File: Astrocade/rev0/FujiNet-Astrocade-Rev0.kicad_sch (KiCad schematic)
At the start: 0 parts

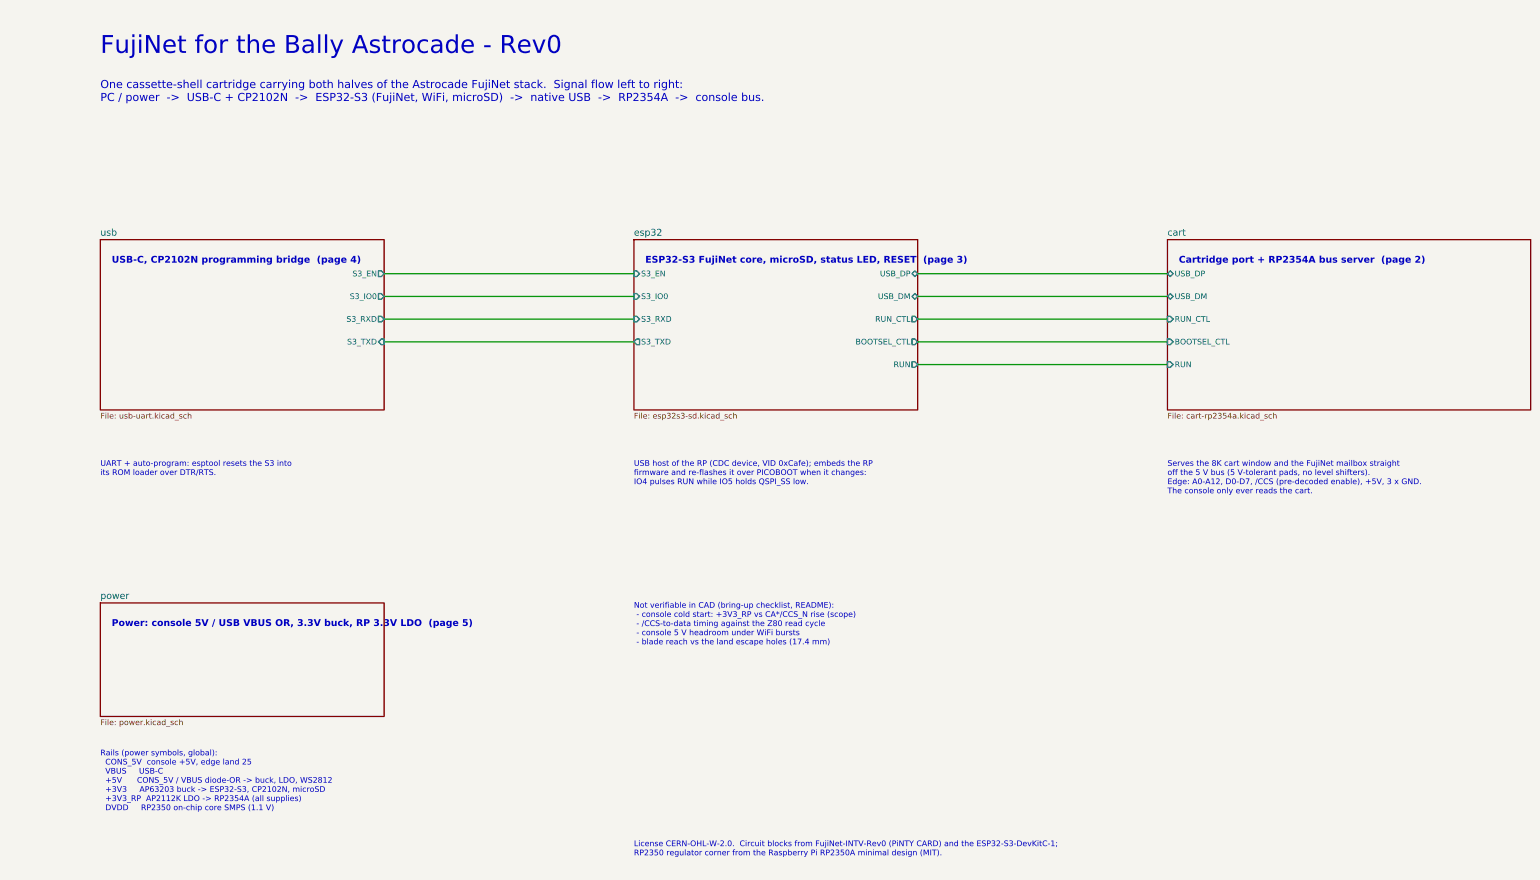
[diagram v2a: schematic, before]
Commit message: Astrocade Rev0: redraw the schematic wired (5200 style), re-audit (#53)
The schematic was readable but disconnected: every edge land and RP GPIO
ended in a label and the RP's decoupling stood in a row away from its pins.
Port the FujiNet-5200 drawing pipeline (sch_draw / sch_draft / sch_place /
netlist) and hand-draw every sheet the way the later carts are drawn:

- root: the board outline at 2:1, each sheet's block over its region, the
  nine inter-sheet signals wired without a crossing
- cart-bus: the 26-land edge straight into the RP2354A's GPIO unit
  (22 parallel wires, no crossings); rp-core: every supply pin wired to
  its own capacitor and rail; fujinet, usb, power: all wired
- RP2354A split into two units; references frozen in tools/refs.lock,
  net names in tools/nets.lock

The routed board is unchanged: tools/sync_pcb_nets.py renames the board's
nets to the new sheet paths (self-checked), sync_pcb_sheets.py re-points
the footprint links. DRC with schematic parity 0/0/0, ERC 0, netlist
parity 74/74, check_nets 182/182; CPL byte-identical, gerbers identical
but for names and dates. build_all.sh now keeps the routed board by
default (LAYOUT=1 re-routes).

Re-audit (design review Part 3, deep review 25/25 gated, datasheets from
the sibling carts): VSENSE divider 100k/150k -> 10k/15k so RP2350-E9 (A2
silicon) cannot hold the serve gate open in a switched-off console (value
change only, same lands). DVDD decoupling, a VBUS pull-down, the activity
LED and the core inductor's stock are Rev1 / bring-up notes.

Co-authored-by: Claude Opus 5.5 <noreply@anthropic.com>
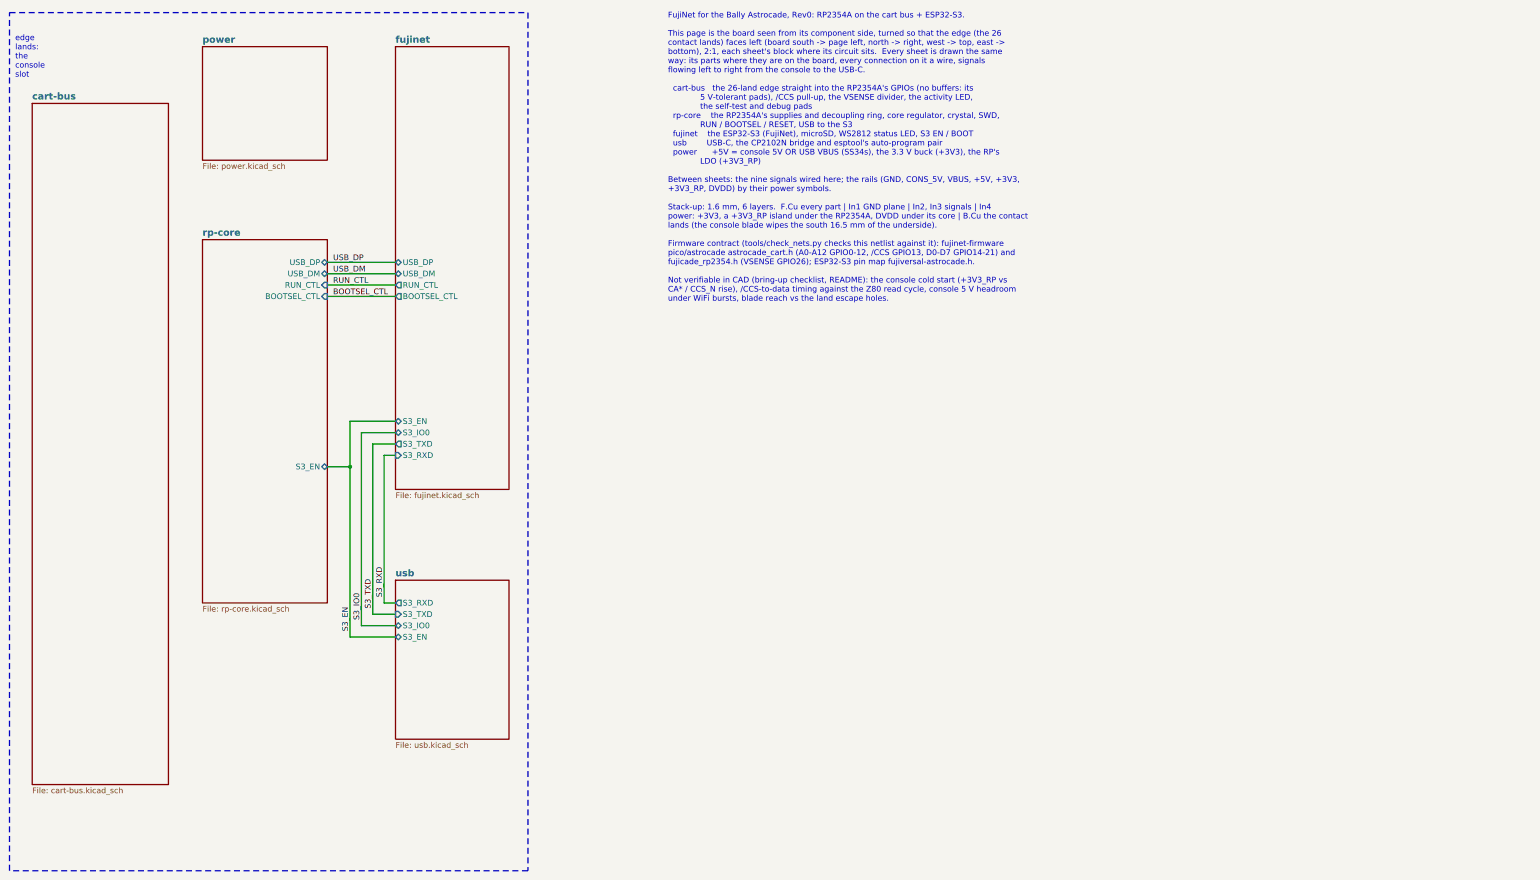
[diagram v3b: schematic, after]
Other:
- removed sheet cart
- removed sheet esp32
- added sheet cart-bus (cart-bus.kicad_sch)
- added sheet fujinet (fujinet.kicad_sch)
- added sheet rp-core (rp-core.kicad_sch)
- sheet usb: file usb-uart.kicad_sch -> usb.kicad_sch
- note added: "FujiNet for the Bally Astrocade, Rev0: RP2354A on the cart bus + ESP32-S3. This page is the board seen from its component side, turned so that the edge (the 26 contact lands) faces left (board south -> page left, north -> right, west -> top, east -> bottom), 2:1, each sheet's block where its circuit sits. Every sheet is drawn the same way: its parts where they are on the board, every connection o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"
- note added: "edge lands: the console slot"
- note removed: "Cartridge port + RP2354A bus server (page 2)"
- note removed: "ESP32-S3 FujiNet core, microSD, status LED, RESET (page 3)"
- note removed: "FujiNet for the Bally Astrocade - Rev0"
- note removed: "License CERN-OHL-W-2.0. Circuit blocks from FujiNet-INTV-Rev0 (PiNTY CARD) and the ESP32-S3-DevKitC-1; RP2350 regulator corner from the Raspberry Pi RP2350A minimal design (MIT)."
- note removed: "Not verifiable in CAD (bring-up checklist, README): - console cold start: +3V3_RP vs CA*/CCS_N rise (scope) - /CCS-to-data timing against the Z80 read cycle - console 5 V headroom under WiFi bursts - blade reach vs the land escape holes (17.4 mm)"
- note removed: "One cassette-shell cartridge carrying both halves of the Astrocade FujiNet stack. Signal flow left to right: PC / power -> USB-C + CP2102N -> ESP32-S3 (FujiNet, WiFi, microSD) -> native USB -> RP2354A -> console bus."
- note removed: "Power: console 5V / USB VBUS OR, 3.3V buck, RP 3.3V LDO (page 5)"
- note removed: "Rails (power symbols, global): CONS_5V console +5V, edge land 25 VBUS USB-C +5V CONS_5V / VBUS diode-OR -> buck, LDO, WS2812 +3V3 AP63203 buck -> ESP32-S3, CP2102N, microSD +3V3_RP AP2112K LDO -> RP2354A (all supplies) DVDD RP2350 on-chip core SMPS (1.1 V)"
- note removed: "Serves the 8K cart window and the FujiNet mailbox straight off the 5 V bus (5 V-tolerant pads, no level shifters). Edge: A0-A12, D0-D7, /CCS (pre-decoded enable), +5V, 3 x GND. The console only ever reads the cart."
- note removed: "UART + auto-program: esptool resets the S3 into its ROM loader over DTR/RTS."
- note removed: "USB host of the RP (CDC device, VID 0xCafe); embeds the RP firmware and re-flashes it over PICOBOOT when it changes: IO4 pulses RUN while IO5 holds QSPI_SS low."
- note removed: "USB-C, CP2102N programming bridge (page 4)"
